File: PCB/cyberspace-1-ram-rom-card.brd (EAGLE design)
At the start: 100 x 50 mm, 15 parts, among them U1 IO PLD, U3 BANK PLD, U4 SRAM 32Kx8, U5 ROM 256K, U6 SRAM 32Kx8

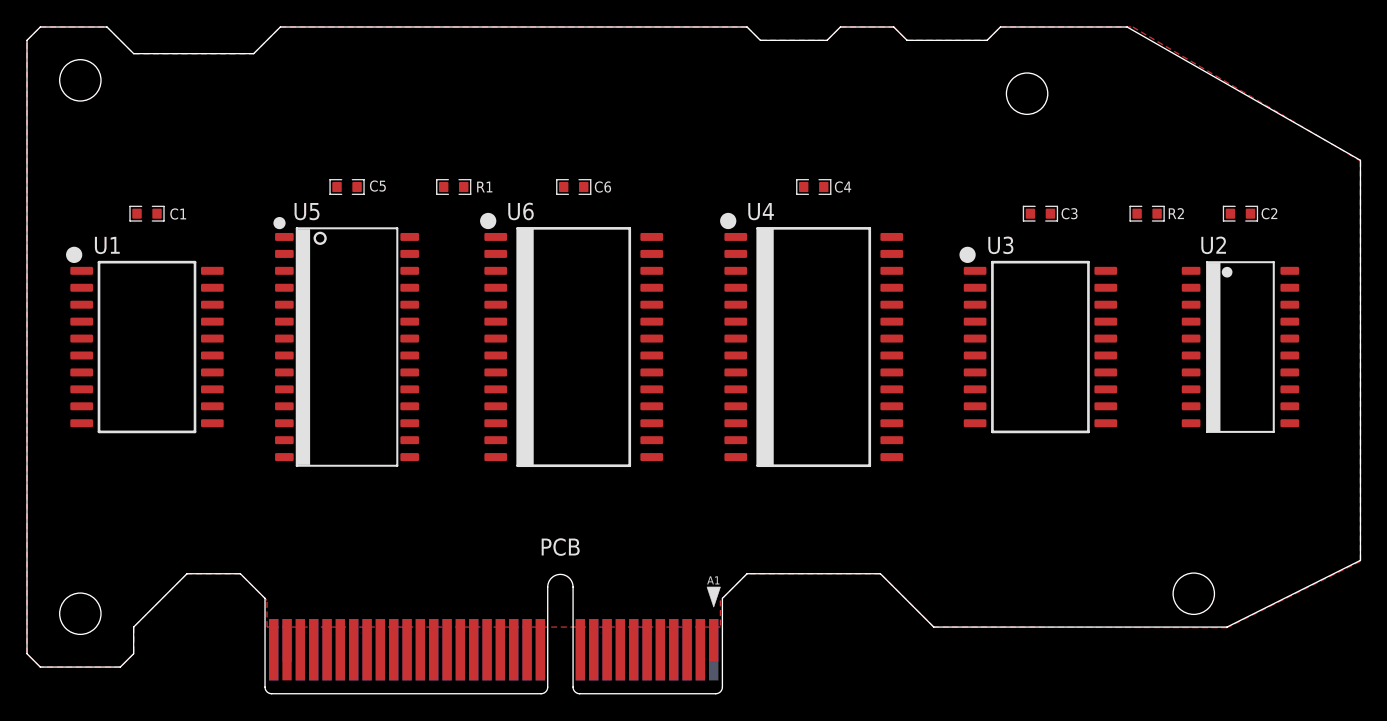
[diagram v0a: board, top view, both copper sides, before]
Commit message: Routed RAM-ROM card. Almost there.
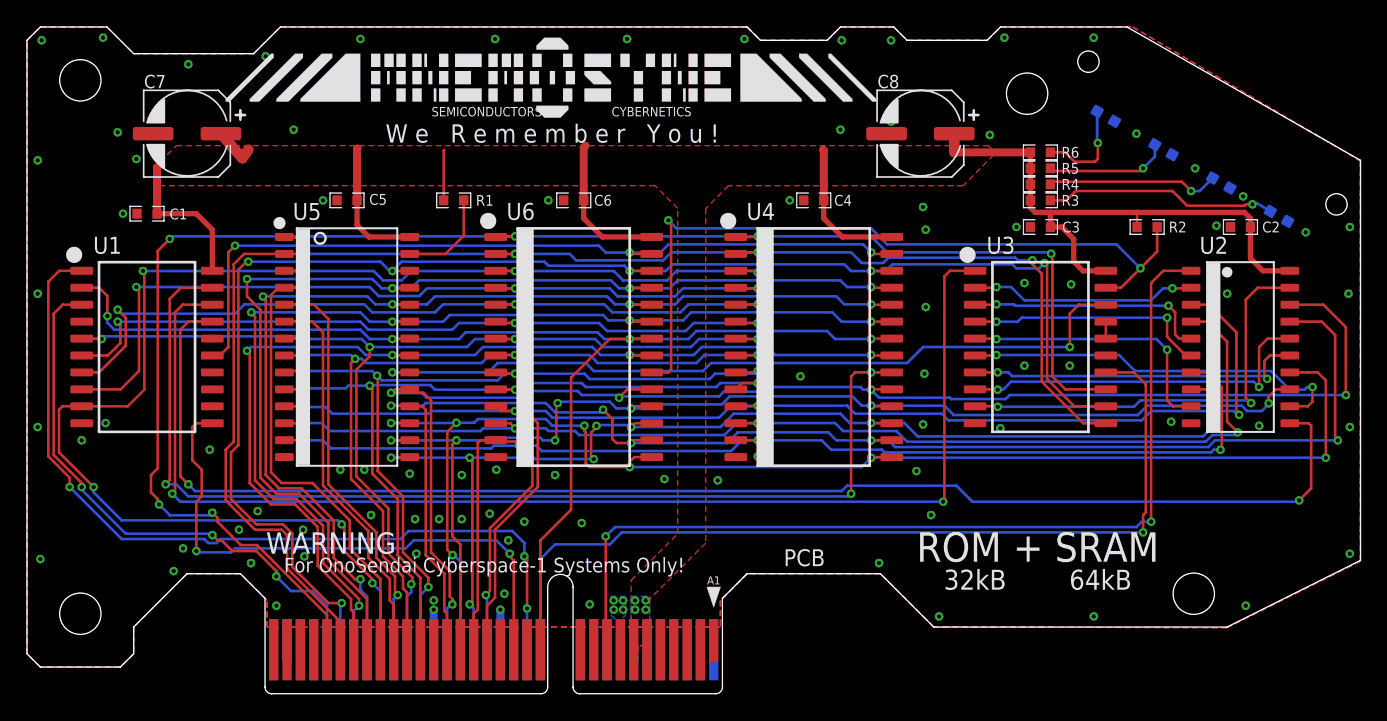
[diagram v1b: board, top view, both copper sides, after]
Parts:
- added C7, C8: 330uF/6.3V, rlc:CAP_ALUM_SMT_6.3
- added LED1, LED2, LED3, LED4: YEL, led:SMD_0603
- added LOGO1: MNEMOSYNE-BRAND-LOGO-06MM-HIGH, gfx-glyphs:MNEMOSYNE-06MM
- added R3, R4, R5, R6: 470R, rlc:0603-RES
- U1: value IO PLD -> 16V8
- U3: value BANK PLD -> 16V8
- moved C2 1.00 mm to (91.0, 35.0)
- moved C3 1.00 mm to (76.0, 35.0)
- moved C4 1.00 mm to (59.0, 37.0)
- moved C5 1.00 mm to (24.0, 37.0)
- moved C6 1.00 mm to (41.0, 37.0)
- moved R1 1.00 mm to (32.0, 37.0)
- moved R2 1.00 mm to (84.0, 35.0)
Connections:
- new net N$2: LED1.A, R3.1
- new net N$3: LED2.A, R4.1
- new net N$5: LED3.A, R5.1
- new net N$6: LED4.A, R6.1
- net GND: now also C7.-, C8.-, LED1.K, LED2.K, LED3.K, LED4.K
- net VCC: now also C7.+, C8.+, R3.2, R4.2, R5.2, R6.2
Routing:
- net A14: track 0.00 -> 124.6 mm, vias 0 -> 7
- net A13: track 0.00 -> 115.0 mm, vias 0 -> 6
- net A12: track 0.00 -> 113.8 mm, vias 0 -> 4
- net D7: track 0.00 -> 111.6 mm, vias 0 -> 5
- net D6: track 0.00 -> 110.7 mm, vias 0 -> 5
- net D0: track 0.00 -> 107.8 mm, vias 0 -> 4
- net !BRE: track 0.00 -> 106.4 mm, vias 0 -> 2
- net D1: track 0.00 -> 106.0 mm, vias 0 -> 5
- net D5: track 0.00 -> 105.4 mm, vias 0 -> 7
- net A7: track 0.00 -> 105.2 mm, vias 0 -> 7
- net D2: track 0.00 -> 99.6 mm, vias 0 -> 4
- net A6: track 0.00 -> 95.9 mm, vias 0 -> 4
- net VCC: track 0.00 -> 94.9 mm, vias 0 -> 4
- net !R: track 0.00 -> 94.4 mm, vias 0 -> 4
- net !B1E: track 0.00 -> 94.2 mm, vias 0 -> 2
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- added copper zone on layer 16, net GND
- added copper zone on layer 1, net VCC
- added copper zone on layer 16, net VCC
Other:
- board text added: "32kB 64kB"
- board text added: "A division of SenseNet Technologies"
- board text added: "Designed in Orbit by Mnemosyne Memory Systems, GmbH"
- board text added: "For OnoSendai Cyberspace-1 Systems Only!"
- board text added: "ROM + SRAM"
- board text added: "WARNING"
